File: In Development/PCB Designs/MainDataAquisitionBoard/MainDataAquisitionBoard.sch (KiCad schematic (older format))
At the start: 22 parts, among them J4 1x24, J5 Teensy 3.6L, J6 Teensy 3.6R, J7 1x24

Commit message: Finished main DAQ PCB
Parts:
- removed J?: Conn_01x06, symbol Connector_Generic:Conn_01x06
- removed J?: Conn_01x04, symbol Connector_Generic:Conn_01x04
- added J1, J2: Conn_01x08, Connector_PinHeader_2.00mm:PinHeader_1x08_P2.00mm_Vertical, symbol Connector_Generic:Conn_01x08
- J10, J3, J8, J9: renamed from J?; footprint (none) -> Connector_PinHeader_2.54mm:PinHeader_1x04_P2.54mm_Vertical
- J11, J12, J13, J14: renamed from J?; footprint (none) -> CustomKiCADLibrary:PinHeader_1x10_P5.08mm_Vertical
- R1, R2, R3, R4, R5, R6, R7, R8: renamed from R?; footprint (none) -> Resistor_THT:R_Axial_DIN0207_L6.3mm_D2.5mm_P7.62mm_Horizontal
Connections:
- net at J13.10 (Pin_10), J13.2 (Pin_2), J13.3 (Pin_3)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: now also J2.3 (Pin_3)
- net at J4.7 (Pin_7), J5.7 (Pin_7): now also J2.8 (Pin_8)
- net at J4.8 (Pin_8), J5.8 (Pin_8): now also J2.4 (Pin_4)
- net at J11.2 (Pin_2), J11.3 (Pin_3), J11.4 (Pin_4)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: now also J2.1 (Pin_1)
- net at J12.7 (Pin_7), J6.13 (Pin_13), J7.13 (Pin_13): no longer J11.6 (Pin_6), R5.2
- net at J6.24 (Pin_24), J7.24 (Pin_24): now also J1.8 (Pin_8)
- net at R3.2: now also J1.4 (Pin_4)
- net at R1.2: now also J1.3 (Pin_3)
- new net: J11.6 (Pin_6), R5.2
- no-connect marks 1 -> 9

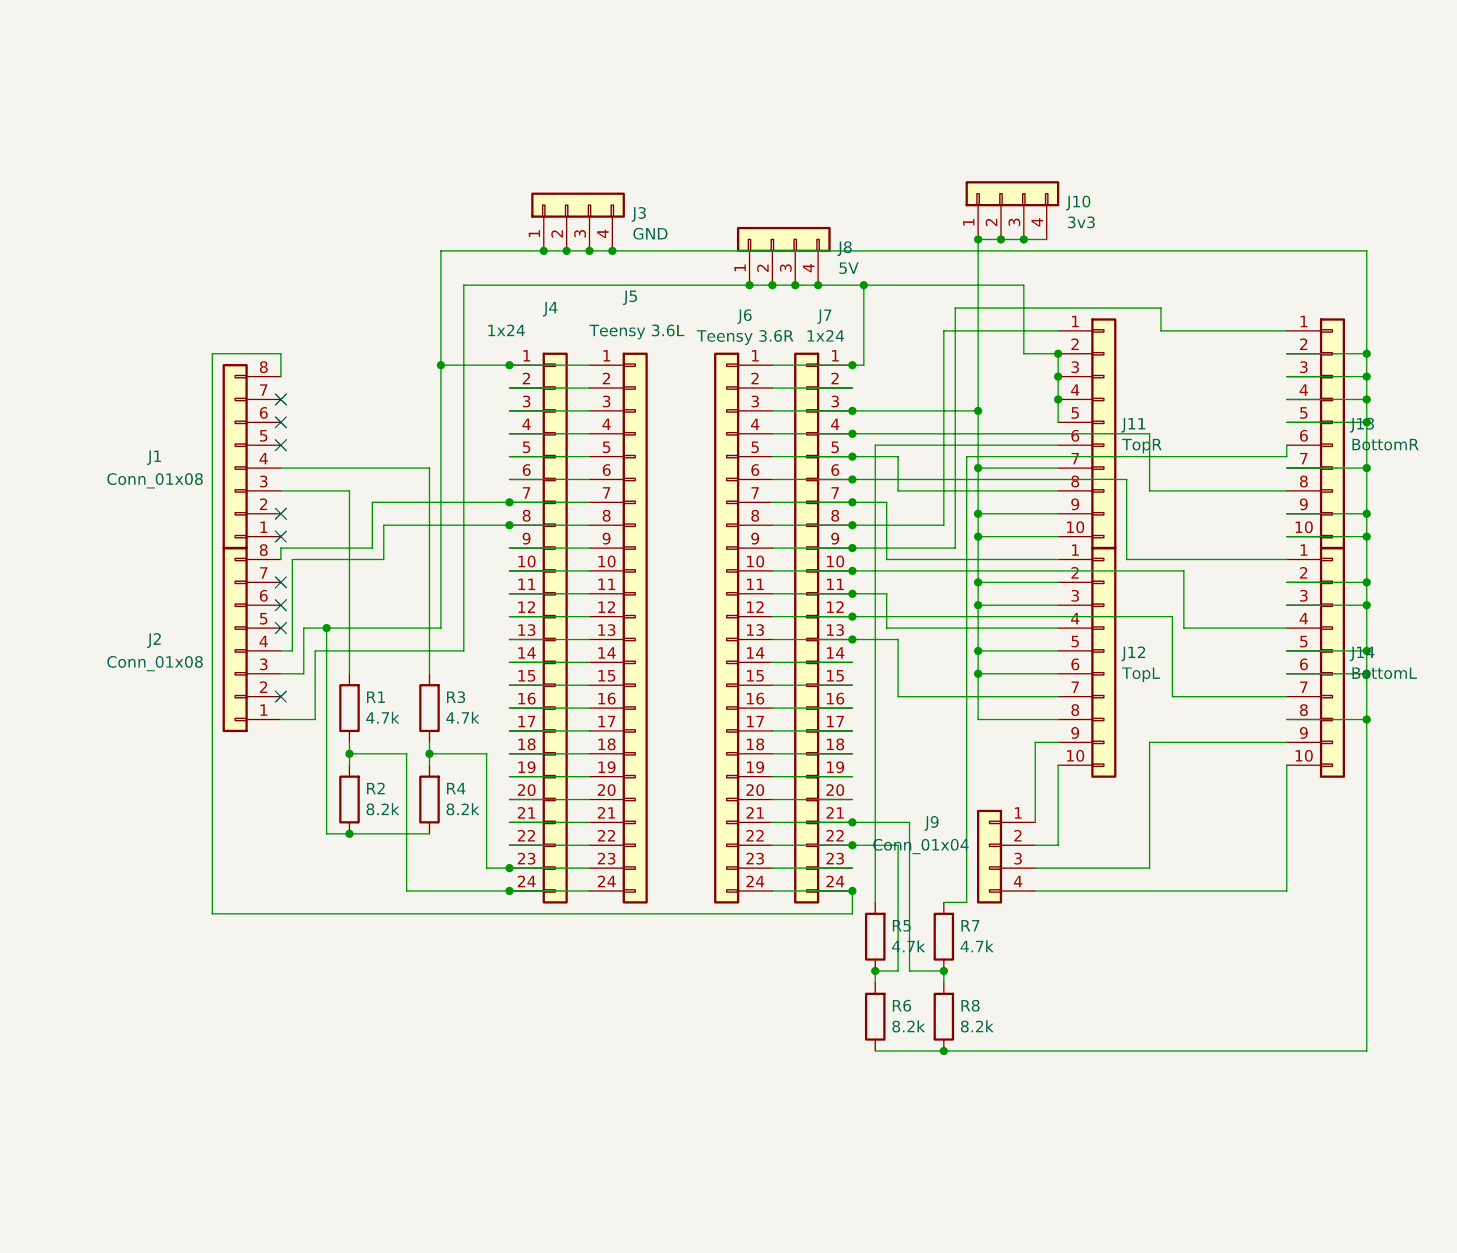
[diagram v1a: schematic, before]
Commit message: Finished eCVT PCB rev 2
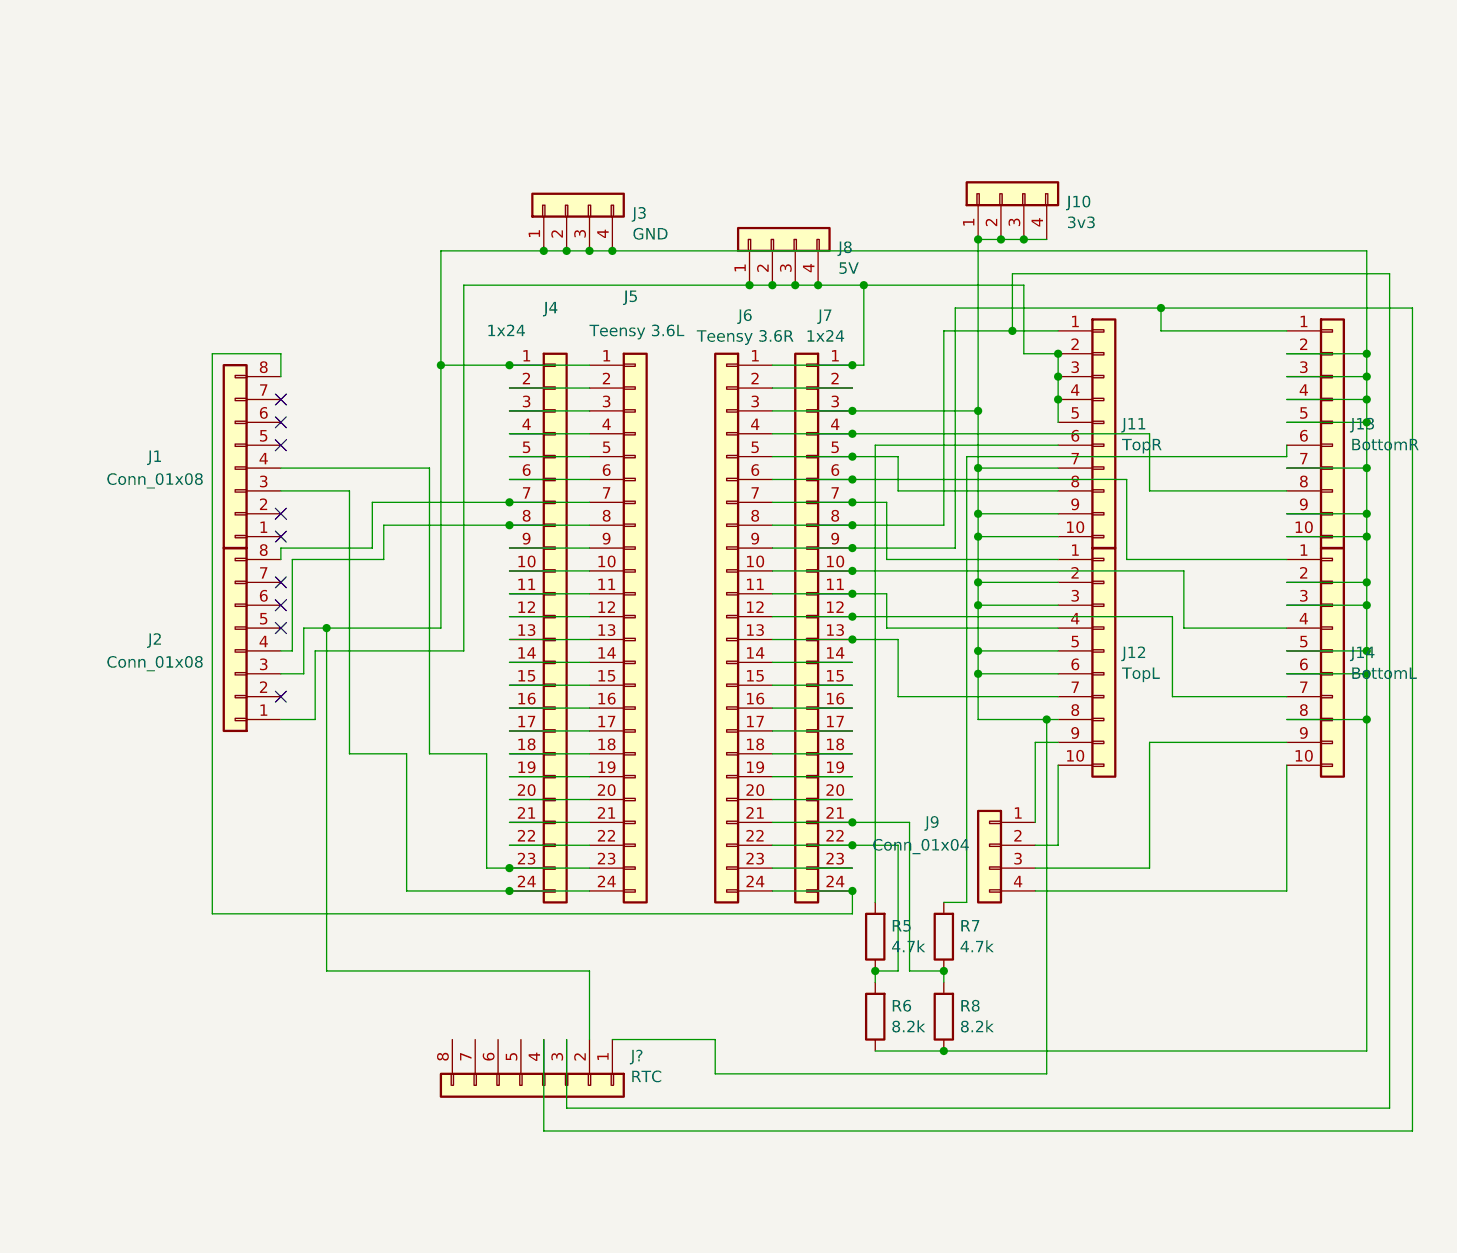
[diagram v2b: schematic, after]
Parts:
- removed R1, R3: 4.7k, Resistor_THT:R_Axial_DIN0207_L6.3mm_D2.5mm_P7.62mm_Horizontal, symbol Device:R
- removed R2, R4: 8.2k, Resistor_THT:R_Axial_DIN0207_L6.3mm_D2.5mm_P7.62mm_Horizontal, symbol Device:R
- added J?: RTC, symbol Connector_Generic:Conn_01x08
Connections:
- net at J13.10 (Pin_10), J13.2 (Pin_2), J13.3 (Pin_3)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: now also J?.2 (Pin_2)
- net at J4.23 (Pin_23), J5.23 (Pin_23): now also J1.4 (Pin_4)
- net at J4.24 (Pin_24), J5.24 (Pin_24): now also J1.3 (Pin_3)
- net at J10.1 (Pin_1), J10.2 (Pin_2), J10.3 (Pin_3)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: now also J?.1 (Pin_1)
- net at J11.1 (Pin_1), J6.8 (Pin_8), J7.8 (Pin_8): now also J?.3 (Pin_3)
- net at J13.1 (Pin_1), J6.9 (Pin_9), J7.9 (Pin_9): now also J?.4 (Pin_4)
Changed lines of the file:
@@
 	3850 3550 4450 3550
 Connection ~ 4450 3550
-$Comp
-L Device:R R1
-U 1 1 5E2406ED
-P 3750 4450
-F 0 "R1" H 3680 4404 50  0000 R CNN
-F 1 "4.7k" H 3680 4495 50  0000 R CNN
-F 2 "Resistor_THT:R_Axial_DIN0207_L6.3mm_D2.5mm_P7.62mm_Horizontal" V 3680 4450 50  0001 C CNN
-F 3 "~" H 3750 4450 50  0001 C CNN
-	1    3750 4450
-	-1   0    0    1
-$EndComp
-$Comp
-L Device:R R2
-U 1 1 5E2442B2
-P 3750 4850
-F 0 "R2" H 3680 4804 50  0000 R CNN
-F 1 "8.2k" H 3680 4895 50  0000 R CNN
-F 2 "Resistor_THT:R_Axial_DIN0207_L6.3mm_D2.5mm_P7.62mm_Horizontal" V 3680 4850 50  0001 C CNN
-F 3 "~" H 3750 4850 50  0001 C CNN
-	1    3750 4850
-	-1   0    0    1
-$EndComp
-$Comp
-L Device:R R3
-U 1 1 5E246794
-P 4100 4450
-F 0 "R3" H 4030 4404 50  0000 R CNN
-F 1 "4.7k" H 4030 4495 50  0000 R CNN
-F 2 "Resistor_THT:R_Axial_DIN0207_L6.3mm_D2.5mm_P7.62mm_Horizontal" V 4030 4450 50  0001 C CNN
-F 3 "~" H 4100 4450 50  0001 C CNN
-	1    4100 4450
-	-1   0    0    1
-$EndComp
-$Comp
-L Device:R R4
-U 1 1 5E248DA4
-P 4100 4850
-F 0 "R4" H 4030 4804 50  0000 R CNN
-F 1 "8.2k" H 4030 4895 50  0000 R CNN
-F 2 "Resistor_THT:R_Axial_DIN0207_L6.3mm_D2.5mm_P7.62mm_Horizontal" V 4030 4850 50  0001 C CNN
-F 3 "~" H 4100 4850 50  0001 C CNN
-	1    4100 4850
-	-1   0    0    1
-$EndComp
-Wire Wire Line
-	3750 4600 3750 4650
-Wire Wire Line
-	4100 4600 4100 4650
 Wire Wire Line
 	4100 4650 4350 4650
@@
 Wire Wire Line
 	4350 5150 4450 5150
-Connection ~ 4100 4650
-Wire Wire Line
-	4100 4650 4100 4700
 Connection ~ 4450 5150
 Wire Wire Line
@@
 Wire Wire Line
 	4000 5250 4450 5250
-Connection ~ 3750 4650
-Wire Wire Line
-	3750 4650 3750 4700
 Connection ~ 4450 5250
-Wire Wire Line
-	3650 4100 3650 5000
-Wire Wire Line
-	3650 5000 3750 5000
 Connection ~ 3650 4100
 Wire Wire Line
 	3650 4100 4150 4100
-Connection ~ 3750 5000
-Wire Wire Line
-	3750 5000 4100 5000
 Wire Wire Line
 	4150 2950 4150 4100
@@
 	6850 3100 6850 3200
 Wire Wire Line
-	6850 2800 6350 2800
+	6850 2800 6650 2800
 Wire Wire Line
 	6350 2800 6350 3650
@@
 	6500 3150 6500 3400
 Wire Wire Line
-	6500 4500 6850 4500
+	6500 4500 6800 4500
 Connection ~ 5950 3150
 Wire Wire Line
@@
 	4100 3400 3450 3400
 Wire Wire Line
-	4100 3400 4100 4300
-Wire Wire Line
 	3750 3500 3450 3500
-Wire Wire Line
-	3750 3500 3750 4300
 Wire Wire Line
 	4250 4200 3600 4200
@@
 	6150 4400 6850 4400
 Connection ~ 5950 4150
+$Comp
+L Connector_Generic:Conn_01x08 J?
+U 1 1 5E279A2E
+P 4600 6100
+F 0 "J?" V 4472 6480 50  0000 L CNN
+F 1 "RTC" V 4563 6480 50  0000 L CNN
+F 2 "" H 4600 6100 50  0001 C CNN
+F 3 "~" H 4600 6100 50  0001 C CNN
+	1    4600 6100
+	0    1    1    0
+$EndComp
+Wire Wire Line
+	6800 4500 6800 6050
+Wire Wire Line
+	6800 6050 5350 6050
+Wire Wire Line
+	5350 6050 5350 5900
+Wire Wire Line
+	5350 5900 4900 5900
+Connection ~ 6800 4500
+Wire Wire Line
+	6800 4500 6850 4500
+Wire Wire Line
+	3650 5600 4800 5600
+Wire Wire Line
+	4800 5600 4800 5900
+Wire Wire Line
+	6650 2800 6650 2550
+Wire Wire Line
+	6650 2550 8300 2550
+Wire Wire Line
+	8300 2550 8300 6200
+Wire Wire Line
+	8300 6200 4700 6200
+Wire Wire Line
+	4700 6200 4700 5900
+Connection ~ 6650 2800
+Wire Wire Line
+	6650 2800 6350 2800
+Wire Wire Line
+	7300 2700 8400 2700
+Wire Wire Line
+	8400 2700 8400 6300
+Wire Wire Line
+	8400 6300 4600 6300
+Wire Wire Line
+	4600 6300 4600 5900
+Connection ~ 7300 2700
+Wire Wire Line
+	4100 3400 4100 4650
+Wire Wire Line
+	3750 3500 3750 4650
+Wire Wire Line
+	3650 4100 3650 5600
 $EndSCHEMATC

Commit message: Finished Main DAQ PCB rev 2
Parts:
- J15: renamed from J?; footprint (none) -> Connector_PinHeader_2.54mm:PinHeader_1x08_P2.54mm_Vertical
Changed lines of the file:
@@
 Connection ~ 5950 4150
 $Comp
-L Connector_Generic:Conn_01x08 J?
+L Connector_Generic:Conn_01x08 J15
 U 1 1 5E279A2E
 P 4600 6100
-F 0 "J?" V 4472 6480 50  0000 L CNN
+F 0 "J15" V 4472 6480 50  0000 L CNN
 F 1 "RTC" V 4563 6480 50  0000 L CNN
-F 2 "" H 4600 6100 50  0001 C CNN
+F 2 "Connector_PinHeader_2.54mm:PinHeader_1x08_P2.54mm_Vertical" H 4600 6100 50  0001 C CNN
 F 3 "~" H 4600 6100 50  0001 C CNN
 	1    4600 6100
